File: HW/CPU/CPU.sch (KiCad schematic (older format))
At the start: 13 parts, among them J1 I2C, J2 SBW, J3 PWR, U1 CONRAD_USB_UART, U2 MSP430G2452, X1 XTAL

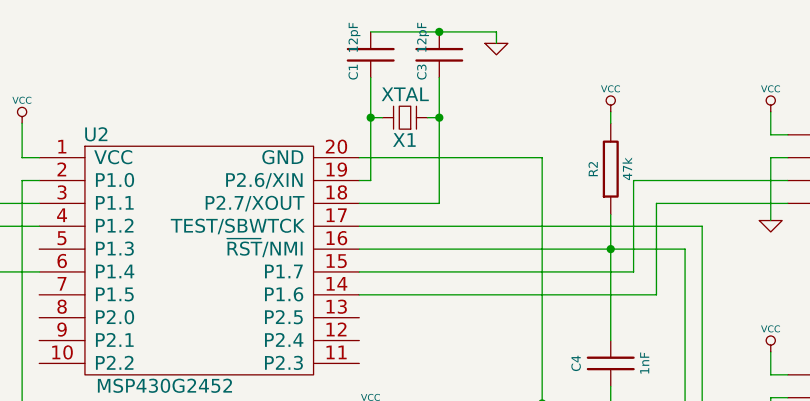
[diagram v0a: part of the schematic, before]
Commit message: CPU board: PCB Design improvement (incomplette)
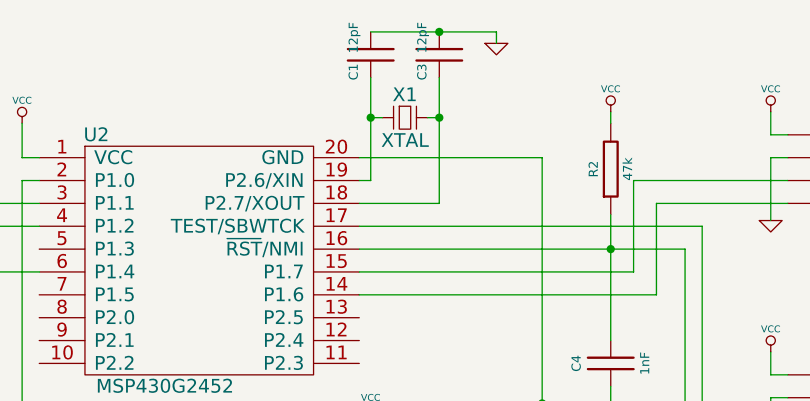
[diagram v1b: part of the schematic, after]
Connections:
- net at C3.2, U2.18 (P2.7/XOUT): now also X1.1; no longer X1.2
- net at C1.2, U2.19 (P2.6/XIN): now also X1.2; no longer X1.1
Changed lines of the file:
@@
 LIBS:conn
 LIBS:device
+LIBS:CPU-cache
 EELAYER 27 0
 EELAYER END
@@
 Sheet 1 1
 Title ""
-Date "5 jan 2014"
+Date "23 jan 2014"
 Rev ""
 Comp ""
@@
 F 3 "~" H 6600 2925 60  0000 C CNN
 	1    6600 2925
-	-1   0    0    1
+	1    0    0    -1
 $EndComp
 $Comp
